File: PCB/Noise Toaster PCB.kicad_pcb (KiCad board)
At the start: 2 copper layers, 132.1 x 68.6 mm, 137 parts, among them J2 Power, J3 AREG, J4 LFO, J5 VCO, J6 VCO, J7 VCLPF, J8 VCA, J9 Amp, Q1 2N5457, Q10 2N3906, Q2 2N3904, Q3 2N3904, Q4 2N3904, Q5 2N3904, Q6 2N3904, Q7 2N5457, Q8 2N5457, Q9 2N5457, U1 LM324, U2 LM324, U3 LM386, X4 WNS

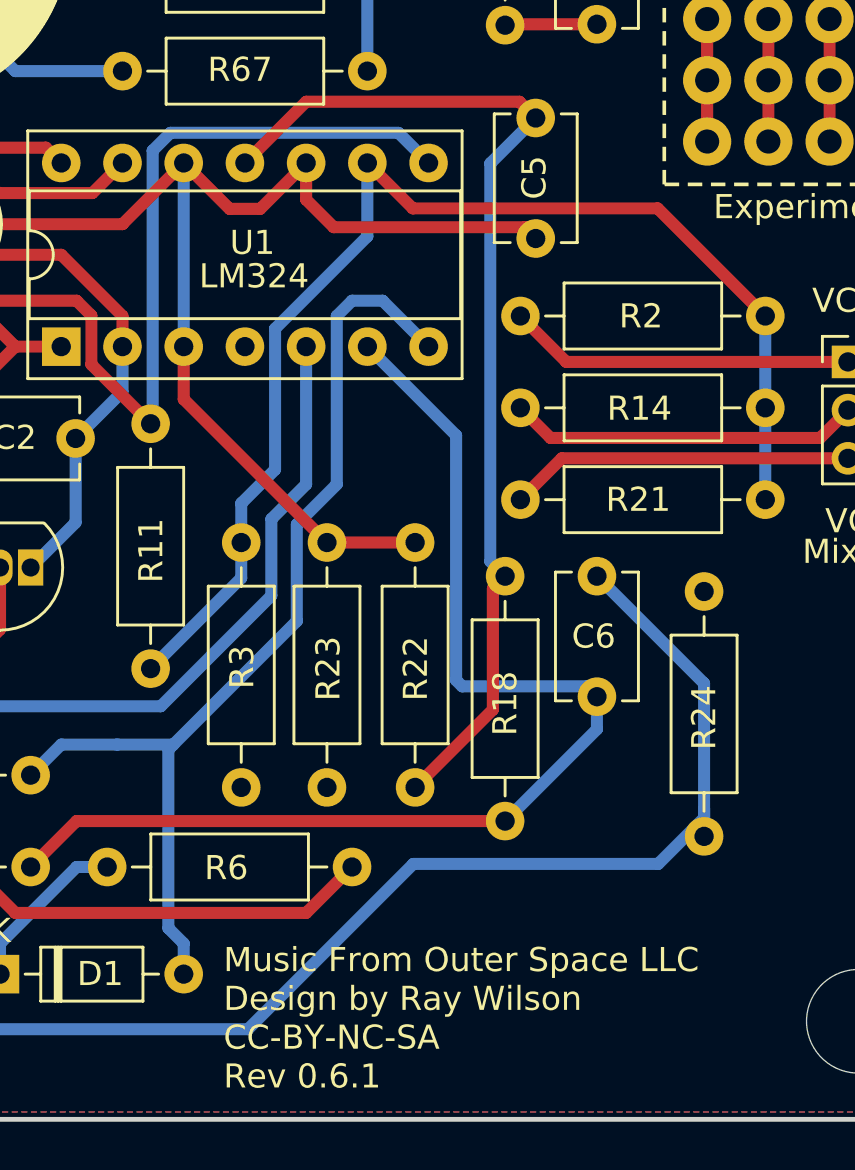
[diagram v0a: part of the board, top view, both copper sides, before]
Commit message: minor revisions to PCB to avoid isolated islands
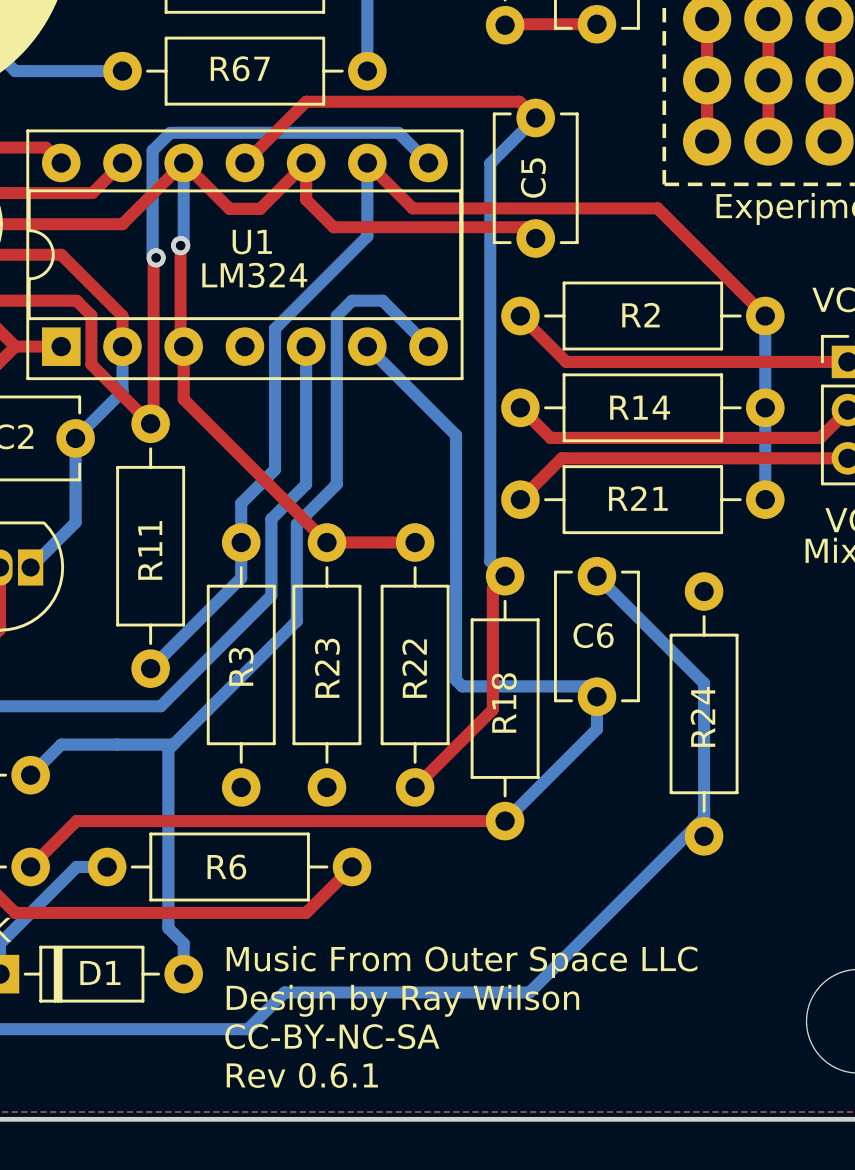
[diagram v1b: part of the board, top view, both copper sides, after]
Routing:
- net Net-(Q3-B): track 45.4 -> 45.7 mm, vias 0 -> 1
- net /G2: track 91.0 -> 91.1 mm, vias 0 -> 1
